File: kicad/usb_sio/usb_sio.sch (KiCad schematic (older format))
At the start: 24 parts, among them CON1 USB, P1 Z80_BUS_PINS, P2 IO_BUS_PINS, P3 CONN_02X05, U1 MCP2200, U2 68B50, U3 74HCT04, U4 1.8432MHz, Y1 12MHz

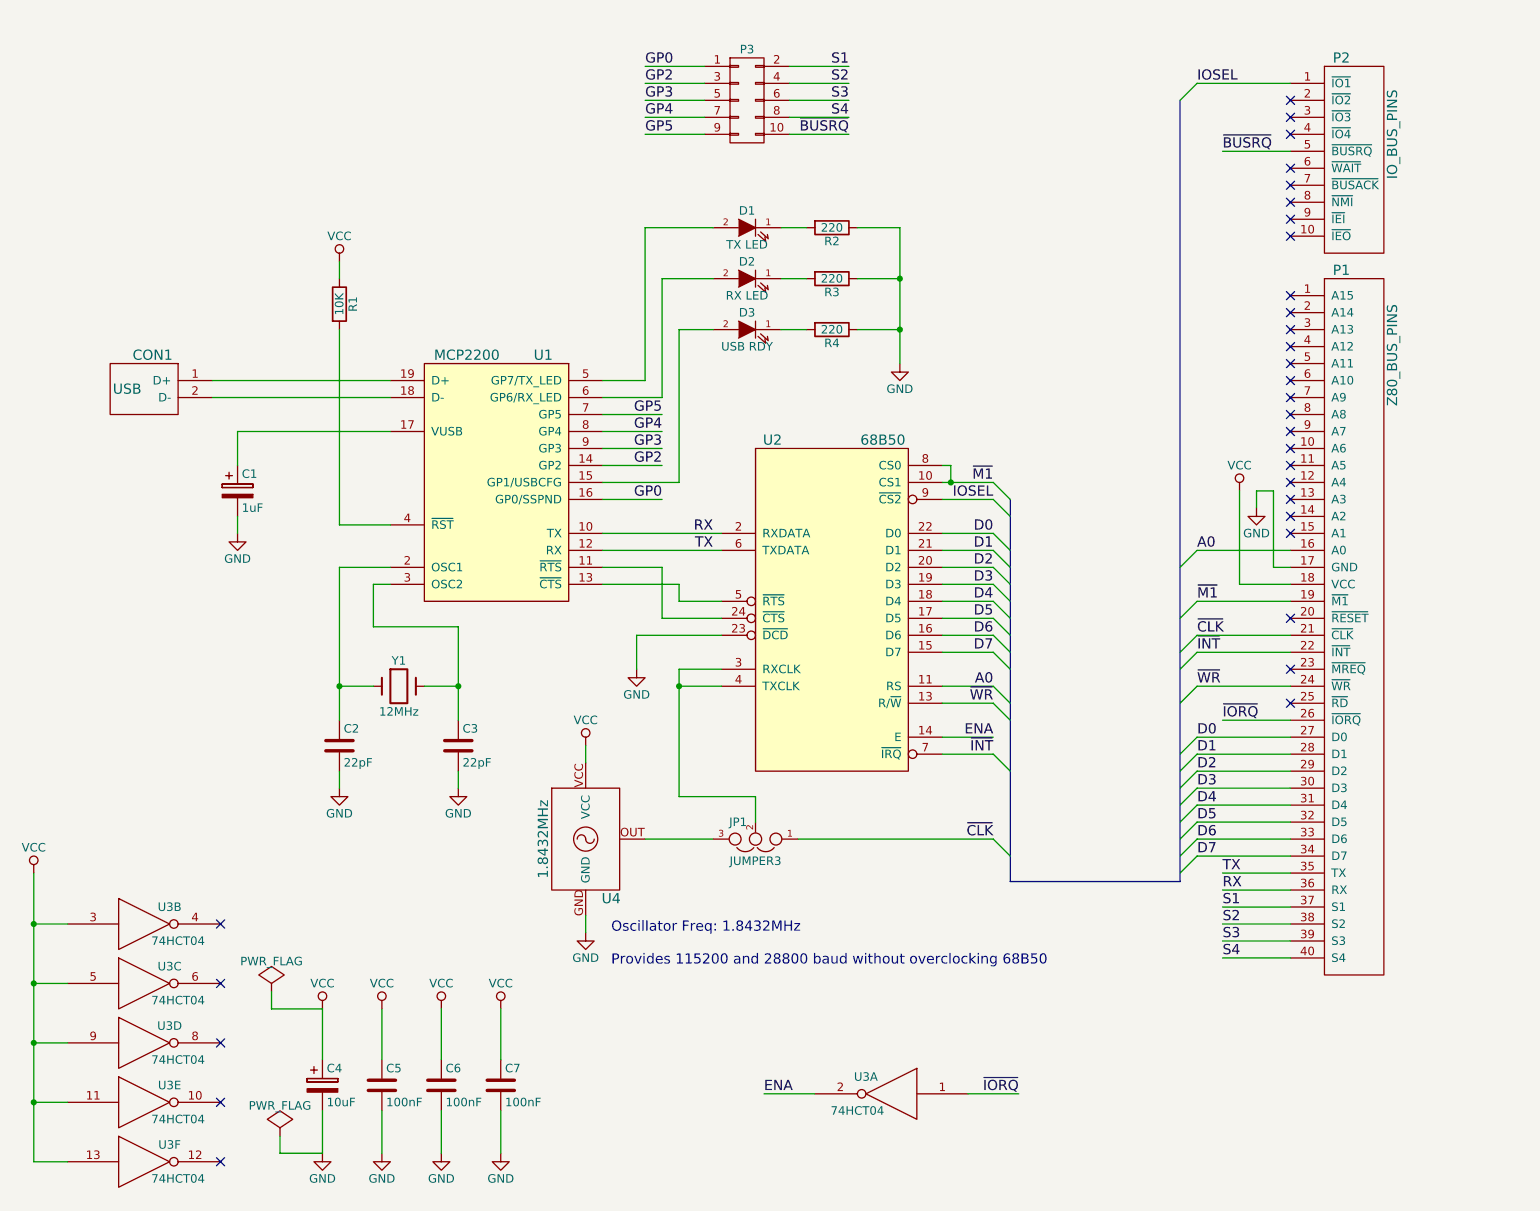
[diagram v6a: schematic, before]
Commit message: Added major work to SIO board.
Coming along nicely. Had to use SOIC for the USB to serial converter. :(
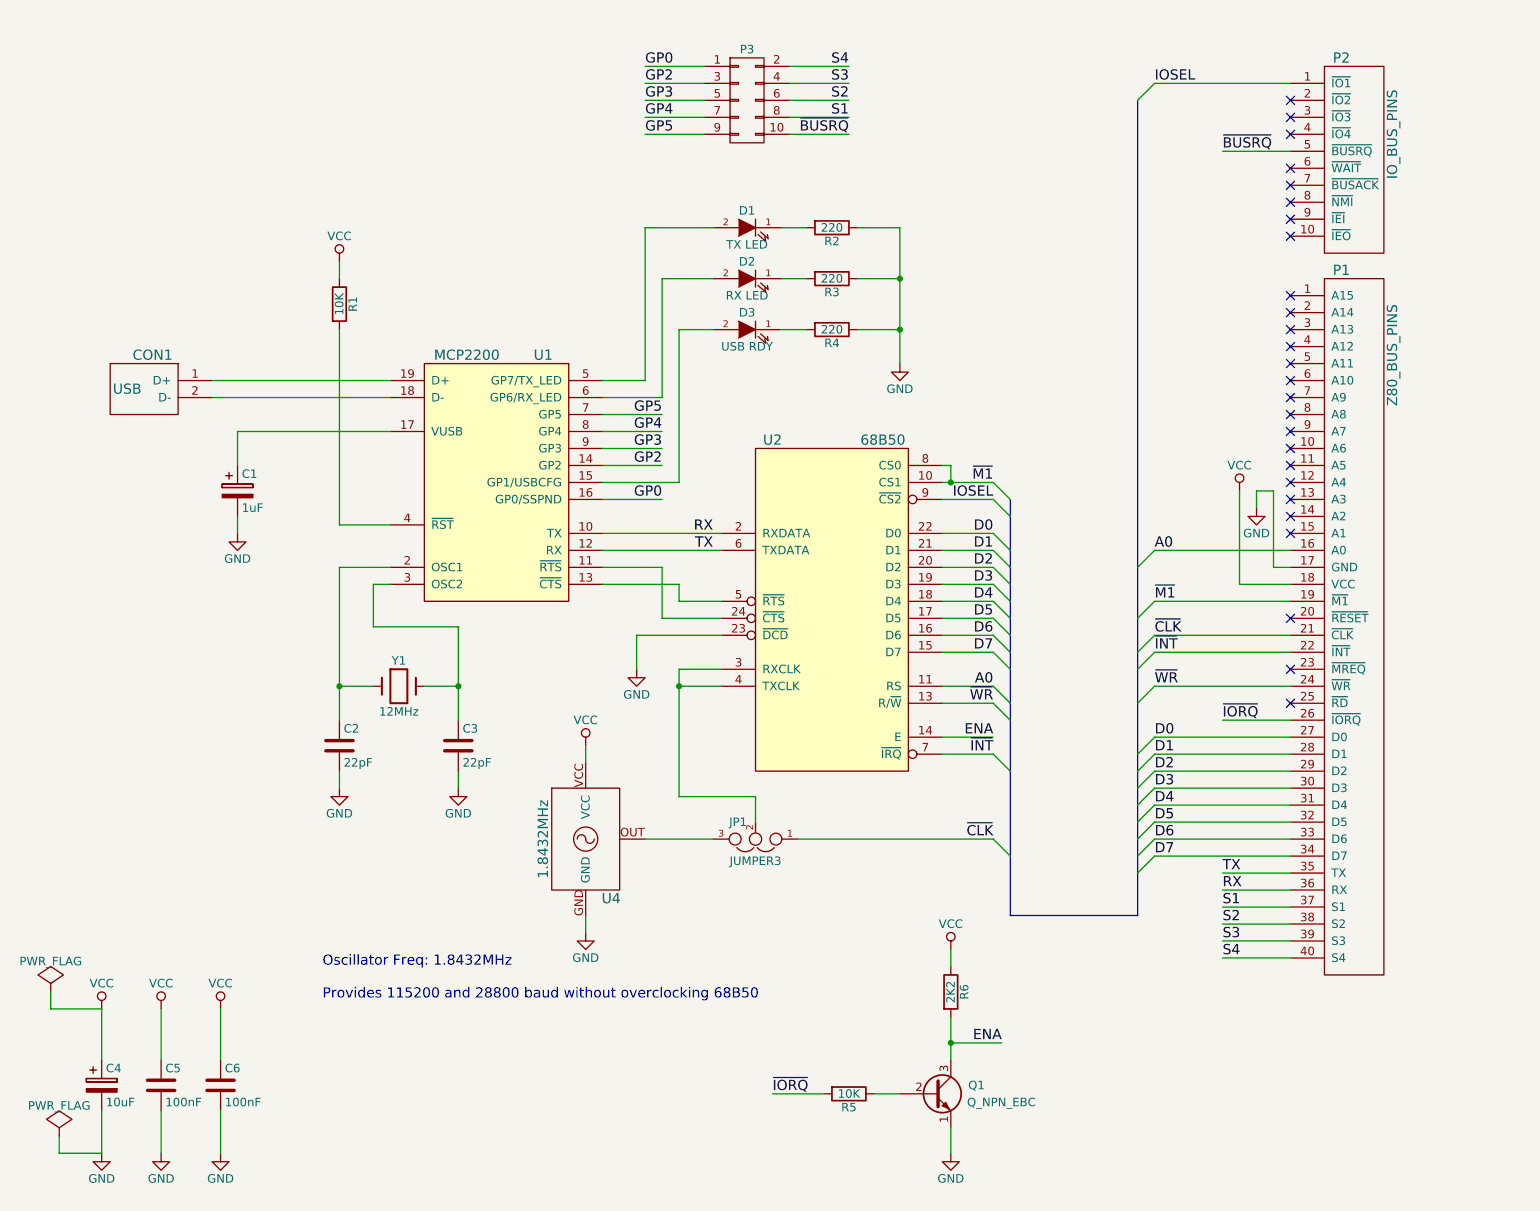
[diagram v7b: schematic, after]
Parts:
- removed C7: 100nF, Capacitors_ThroughHole:C_Disc_D3_P2.5, symbol C
- removed U3: 74HCT04, Housings_DIP:DIP-14_W7.62mm_LongPads, symbol 74HCT04
- added Q1: Q_NPN_EBC, TO_SOT_Packages_THT:TO-92_Molded_Narrow, symbol Q_NPN_EBC
- added R5: 10K, Resistors_ThroughHole:Resistor_Horizontal_RM10mm, symbol R
- added R6: 2K2, Resistors_ThroughHole:Resistor_Horizontal_RM10mm, symbol R
- C2, C3: footprint Capacitors_ThroughHole:C_Disc_D7.5_P5 -> Capacitors_ThroughHole:C_Disc_D3_P2.5
- CON1: footprint Pin_Headers:Pin_Header_Angled_1x02 -> nrc2016:Pin_Header_Angled_1x02_nrc2016
- P1: footprint Pin_Headers:Pin_Header_Angled_1x40 -> nrc2016:Pin_Header_Angled_1x40_nrc2016
- P2: footprint Pin_Headers:Pin_Header_Angled_1x10 -> nrc2016:Pin_Header_Angled_1x10_nrc2016
- U1: footprint Housings_DIP:DIP-20_W7.62mm_LongPads -> Housings_SOIC:SOIC-20W_7.5x12.8mm_Pitch1.27mm
- U2: footprint Housings_DIP:DIP-24_W10.16mm_LongPads -> Housings_DIP:DIP-24_W15.24mm_LongPads
- U4: footprint Oscillators:OSC_DIP8 -> nrc2016:OSC_MULTIPACKAGE_DIP
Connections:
- net ENA: now also Q1.3 (C), R6.2
- net GND: now also Q1.1 (E)
- net S1: now also P3.8 (P8); no longer P3.2 (P2)
- net S2: now also P3.6 (P6); no longer P3.4 (P4)
- net S3: now also P3.4 (P4); no longer P3.6 (P6)
- net S4: now also P3.2 (P2); no longer P3.8 (P8)
- net VCC: now also R6.1
- net ~IORQ: now also R5.2
- new net: Q1.2 (B), R5.1
- no-connect marks 31 -> 26
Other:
- moved on the sheet: C4, C5, C6

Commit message: Update to the SIO board, layout complete!
Added headers for selecting the IOSEL to use, added logo, silkscreen
legends etc.
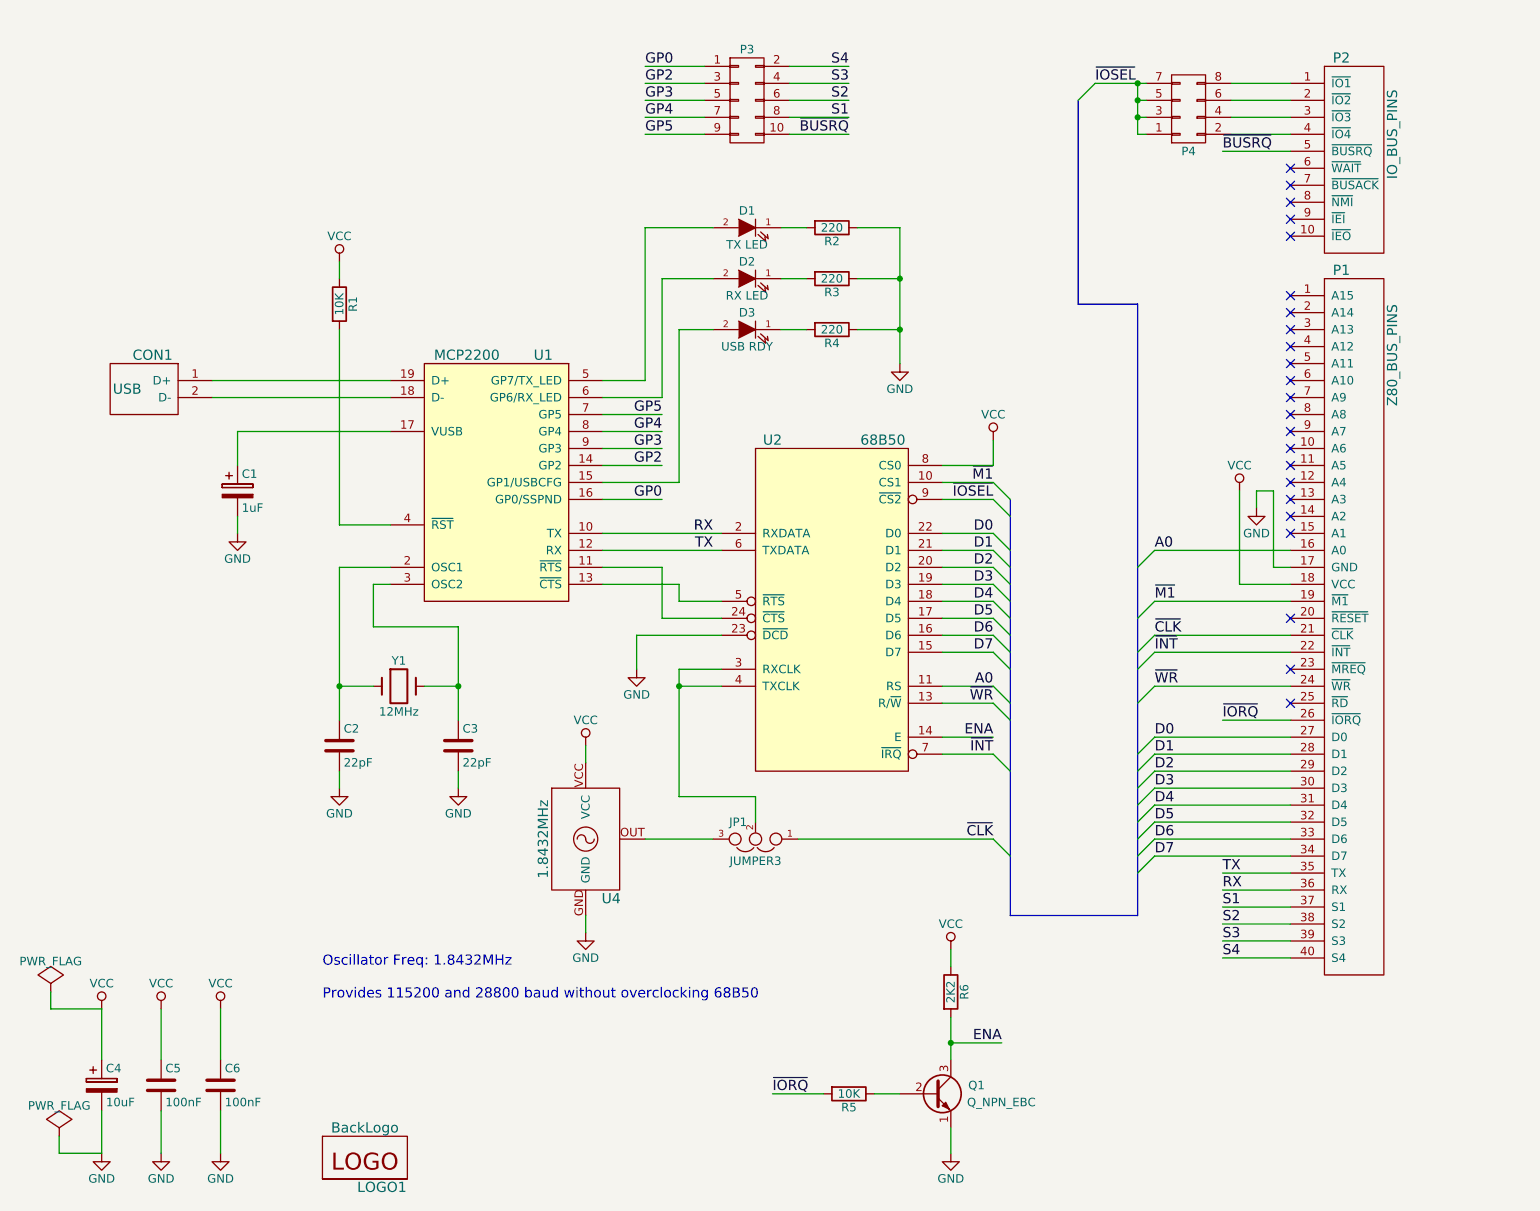
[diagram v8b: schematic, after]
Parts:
- added LOGO1: BackLogo, nrc2016_logo:nrc2016_top_logo_1600, symbol FrontLogo
- added P4: CONN_02X04, Pin_Headers:Pin_Header_Straight_2x04, symbol CONN_02X04
- D1, D2, D3: footprint LEDs:LED-5MM -> LEDs:LED-3MM
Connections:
- net VCC: now also U2.8 (CS0)
- net ~M1: no longer U2.8 (CS0)
- net at P2.2 (~IO2): now also P4.6 (P6)
- net at P2.3 (~IO3): now also P4.4 (P4)
- net at P2.4 (~IO4): now also P4.2 (P2)
- net IOSEL: no longer names the net of P2.1 (~IO1)
- net IOSEL: now also P4.8 (P8); no longer U2.9 (~CS2)
- new net ~IOSEL: P4.1 (P1), P4.3 (P3), P4.5 (P5), P4.7 (P7), U2.9 (~CS2)
- no-connect marks 26 -> 23
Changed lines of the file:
@@
 ~M1
 Text Label 6450 3500 2    60   ~ 0
-IOSEL
+~IOSEL
 Text Label 6450 4600 2    60   ~ 0
 A0
@@
 $EndComp
 Entry Wire Line
-	7300 1150 7400 1050
-Text Label 7400 1050 0    60   ~ 0
-IOSEL
+	6950 1150 7050 1050
+Text Label 7050 1050 0    60   ~ 0
+~IOSEL
 NoConn ~ 8200 2300
 NoConn ~ 8200 2400
@@
 Text Label 7400 3800 0    60   ~ 0
 A0
-NoConn ~ 8200 1150
-NoConn ~ 8200 1250
-NoConn ~ 8200 1350
 NoConn ~ 8200 1550
 NoConn ~ 8200 1650
@@
 F 0 "D2" H 5000 2300 50  0000 C CNN
 F 1 "RX LED" H 5000 2100 50  0000 C CNN
-F 2 "LEDs:LED-5MM" H 5000 2200 50  0001 C CNN
+F 2 "LEDs:LED-3MM" H 5000 2200 50  0001 C CNN
 F 3 "" H 5000 2200 50  0000 C CNN
 	1    5000 2200
@@
 F 0 "D3" H 5000 2600 50  0000 C CNN
 F 1 "USB RDY" H 5000 2400 50  0000 C CNN
-F 2 "LEDs:LED-5MM" H 5000 2500 50  0001 C CNN
+F 2 "LEDs:LED-3MM" H 5000 2500 50  0001 C CNN
 F 3 "" H 5000 2500 50  0000 C CNN
 	1    5000 2500
@@
 F 0 "D1" H 5000 2000 50  0000 C CNN
 F 1 "TX LED" H 5000 1800 50  0000 C CNN
-F 2 "LEDs:LED-5MM" H 5000 1900 50  0001 C CNN
+F 2 "LEDs:LED-3MM" H 5000 1900 50  0001 C CNN
 F 3 "" H 5000 1900 50  0000 C CNN
 	1    5000 1900
@@
 	6150 5000 6450 5000
 Wire Wire Line
-	6150 3400 6450 3400
-Wire Wire Line
 	6150 3500 6450 3500
 Wire Wire Line
@@
 	5300 5500 6450 5500
 Wire Bus Line
-	7300 5950 7300 1150
-Wire Wire Line
-	8200 1050 7400 1050
+	7300 5950 7300 2350
+Wire Wire Line
+	7350 1050 7050 1050
 Wire Wire Line
 	7400 3800 8200 3800
 Wire Wire Line
 	6150 4900 6450 4900
-Wire Wire Line
-	6150 3300 6200 3300
-Wire Wire Line
-	6200 3300 6200 3400
-Connection ~ 6200 3400
 Wire Wire Line
 	5200 1900 5350 1900
@@
 Wire Wire Line
 	5750 7000 5900 7000
+$Comp
+L FrontLogo LOGO1
+U 1 1 57D7E267
+P 2500 7500
+F 0 "LOGO1" H 2850 7450 60  0000 C CNN
+F 1 "BackLogo" H 2750 7800 60  0000 C CNN
+F 2 "nrc2016_logo:nrc2016_top_logo_1600" H 2500 7500 60  0001 C CNN
+F 3 "" H 2500 7500 60  0000 C CNN
+	1    2500 7500
+	1    0    0    -1
+$EndComp
+Wire Wire Line
+	6450 3400 6150 3400
+Wire Wire Line
+	6150 3300 6450 3300
+Wire Wire Line
+	6450 3300 6450 3150
+$Comp
+L VCC #PWR021
+U 1 1 57D800D0
+P 6450 3150
+F 0 "#PWR021" H 6450 3000 50  0001 C CNN
+F 1 "VCC" H 6450 3300 50  0000 C CNN
+F 2 "" H 6450 3150 50  0000 C CNN
+F 3 "" H 6450 3150 50  0000 C CNN
+	1    6450 3150
+	1    0    0    -1
+$EndComp
+$Comp
+L CONN_02X04 P4
+U 1 1 57D80423
+P 7600 1200
+F 0 "P4" H 7600 1450 50  0000 C CNN
+F 1 "CONN_02X04" H 7600 950 50  0001 C CNN
+F 2 "Pin_Headers:Pin_Header_Straight_2x04" H 7600 0   50  0001 C CNN
+F 3 "" H 7600 0   50  0000 C CNN
+	1    7600 1200
+	1    0    0    1
+$EndComp
+Wire Wire Line
+	7300 1050 7300 1350
+Wire Wire Line
+	7300 1350 7350 1350
+Connection ~ 7300 1050
+Wire Wire Line
+	7350 1250 7300 1250
+Connection ~ 7300 1250
+Wire Wire Line
+	7350 1150 7300 1150
+Connection ~ 7300 1150
+Wire Wire Line
+	7850 1050 8200 1050
+Wire Wire Line
+	7850 1150 8200 1150
+Wire Wire Line
+	7850 1250 8200 1250
+Wire Wire Line
+	7850 1350 8200 1350
+Wire Bus Line
+	6950 1150 6950 2350
+Wire Bus Line
+	6950 2350 7300 2350
 $EndSCHEMATC
